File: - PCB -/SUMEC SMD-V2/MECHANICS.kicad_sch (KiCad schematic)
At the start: 9 parts, among them J1 Conn_01x04_Pin, J3 Conn_01x03_Pin, J4 Conn_01x02, SW1 SW_Push

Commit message: cleanup
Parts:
- removed J4: Conn_01x02, Connector_PinHeader_2.54mm:PinHeader_1x02_P2.54mm_Vertical, symbol Connector_Generic:Conn_01x02
- added SW4: SW_DPDT_x2, Connector_PinHeader_2.54mm:PinHeader_1x03_P2.54mm_Vertical, symbol Switch:SW_DPDT_x2
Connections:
- net +8V: now also SW4.2 (B)
- net VBATT: now also SW4.1 (A)
- no-connect marks 0 -> 1
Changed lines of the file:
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@@
     (company "SPŠ NA PROSEKU")
   )
-  (wire (pts (xy 172.72 62.23) (xy 172.72 64.77))
-    (stroke (width 0) (type default))
-  )
+  (no_connect (at 190.5 69.85))
   (wire (pts (xy 173.99 114.3) (xy 182.88 114.3))
     (stroke (width 0) (type default))
   )
-  (wire (pts (xy 172.72 67.31) (xy 175.26 67.31))
+  (wire (pts (xy 187.96 64.77) (xy 185.42 64.77))
     (stroke (width 0) (type default))
   )
@@
     (stroke (width 0) (type default))
   )
+  (wire (pts (xy 173.99 67.31) (xy 175.26 67.31))
+    (stroke (width 0) (type default))
+  )
   (polyline (pts (xy 148.59 44.45) (xy 153.67 44.45))
     (stroke (width 0) (type default))
@@
     (stroke (width 0) (type default))
   )
-  (wire (pts (xy 172.72 64.77) (xy 175.26 64.77))
-    (stroke (width 0) (type default))
-  )
   (wire (pts (xy 173.99 132.08) (xy 185.42 132.08))
     (stroke (width 0) (type default))
@@
   )
   (polyline (pts (xy 64.77 148.59) (xy 143.51 148.59))
+    (stroke (width 0) (type default))
+  )
+  (wire (pts (xy 190.5 69.85) (xy 185.42 69.85))
     (stroke (width 0) (type default))
   )
@@
     (effects (font (size 1.27 1.27) italic) (justify left bottom))
   )
-  (global_label "VBATT" (shape input) (at 172.72 67.31 180) (fields_autoplaced)
-    (effects (font (size 1 1) (color 0 0 0 1)) (justify right))
-    (property "Intersheetrefs" "${INTERSHEET_REFS}" (at 166.1941 67.31 0)
-      (effects (font (size 1.27 1.27)) (justify right) hide)
+  (global_label "VBATT" (shape input) (at 187.96 64.77 0) (fields_autoplaced)
+    (effects (font (size 1 1) (color 0 0 0 1)) (justify left))
+    (property "Intersheetrefs" "${INTERSHEET_REFS}" (at 194.4859 64.77 0)
+      (effects (font (size 1.27 1.27)) (justify left) hide)
     )
   )
@@
     )
   )
-  (symbol (lib_id "power:+8V") (at 172.72 62.23 0) (unit 1)
+  (symbol (lib_id "Switch:SW_DPDT_x2") (at 180.34 67.31 0) (unit 1)
+    (in_bom yes) (on_board yes) (dnp no)
+    (property "Reference" "SW4" (at 180.34 59.69 0)
+      (effects (font (size 1.27 1.27)))
+    )
+    (property "Value" "SW_DPDT_x2" (at 180.34 62.23 0)
+      (effects (font (size 1.27 1.27)))
+    )
+    (property "Footprint" "Connector_PinHeader_2.54mm:PinHeader_1x03_P2.54mm_Vertical" (at 180.34 67.31 0)
+      (effects (font (size 1.27 1.27)) hide)
+    )
+    (property "Datasheet" "~" (at 180.34 67.31 0)
+      (effects (font (size 1.27 1.27)) hide)
+    )
+    (pin "1")
+    (pin "2")
+    (pin "3")
+    (pin "4")
+    (pin "5")
+    (pin "6")
+    (instances
+      (project "sumec"
+        (path "/fc70a1a8-ed7c-4a0f-9b1a-f23293528385/05a35bad-c108-46ad-8f95-76319a60a14f"
+          (reference "SW4") (unit 1)
+        )
+      )
+    )
+  )
+  (symbol (lib_id "power:+8V") (at 173.99 67.31 90) (unit 1)
     (in_bom yes) (on_board yes) (dnp no) (fields_autoplaced)
-    (property "Reference" "#PWR02" (at 172.72 66.04 0)
-      (effects (font (size 1.27 1.27)) hide)
-    )
-    (property "Value" "+8V" (at 172.72 58.42 0)
-      (effects (font (size 1.27 1.27)))
-    )
-    (property "Footprint" "" (at 172.72 62.23 0)
-      (effects (font (size 1.27 1.27)) hide)
-    )
-    (property "Datasheet" "" (at 172.72 62.23 0)
+    (property "Reference" "#PWR02" (at 177.8 67.31 0)
+      (effects (font (size 1.27 1.27)) hide)
+    )
+    (property "Value" "+8V" (at 170.18 67.945 90)
+      (effects (font (size 1.27 1.27)) (justify left))
+    )
+    (property "Footprint" "" (at 173.99 67.31 0)
+      (effects (font (size 1.27 1.27)) hide)
+    )
+    (property "Datasheet" "" (at 173.99 67.31 0)
       (effects (font (size 1.27 1.27)) hide)
     )
@@
         )
       )
-    )
-  )
-  (symbol (lib_id "Connector_Generic:Conn_01x02") (at 180.34 64.77 0) (unit 1)
-    (in_bom yes) (on_board yes) (dnp no) (fields_autoplaced)
-    (property "Reference" "J4" (at 182.88 65.405 0)
-      (effects (font (size 1.27 1.27)) (justify left))
-    )
-    (property "Value" "Conn_01x02" (at 182.88 67.945 0)
-      (effects (font (size 1.27 1.27)) (justify left))
-    )
-    (property "Footprint" "Connector_PinHeader_2.54mm:PinHeader_1x02_P2.54mm_Vertical" (at 180.34 64.77 0)
-      (effects (font (size 1.27 1.27)) hide)
-    )
-    (property "Datasheet" "~" (at 180.34 64.77 0)
-      (effects (font (size 1.27 1.27)) hide)
-    )
-    (pin "1")
-    (pin "2")
-    (instances
-      (project "sumec"
-        (path "/fc70a1a8-ed7c-4a0f-9b1a-f23293528385/05a35bad-c108-46ad-8f95-76319a60a14f"
-          (reference "J4") (unit 1)
-        )
-      )

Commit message: sumec SMD V2 schematic update
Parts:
- removed H? (x4): MountingHole M3, MountingHole:MountingHole_3.2mm_M3_ISO7380_Pad, symbol Mechanical:MountingHole
- removed J3: Conn_01x03_Pin, Connector_PinSocket_2.54mm:PinSocket_1x03_P2.54mm_Vertical, symbol Connector:Conn_01x03_Pin
- added H1, H2, H3, H4: MountingHole_Pad, MountingHole:MountingHole_3.2mm_M3_Pad, symbol Mechanical:MountingHole_Pad
- J1: footprint Connector_PinHeader_2.54mm:PinHeader_1x04_P2.54mm_Vertical -> (none)
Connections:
- net GND: now also H1.1, H2.1, H3.1, H4.1
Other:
- note added: "CONNECTORS"
- note added: "Main switch is at the top of the robot for easy access to the switch."
- note added: "TEST BUTTON"
- note added: "lepsi konektory nez arduino bullshit"
- note added: "vlastni 2,54 footprint a 3D model"
- note removed: "Main switch is connected via two wires for easy access."
- note removed: "PADY a PROKOVY"
- note removed: "Pads for connecting motors and rivets"
- note removed: "TEST TLAČITKO"
- moved on the sheet: J1, J?

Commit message: pcb schematic update
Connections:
- net +8V: no longer names the net of SW4.2 (B)
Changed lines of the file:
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@@
-    )
-  )
-  (symbol (lib_id "power:+8V") (at 173.99 67.31 90) (unit 1)
-    (in_bom yes) (on_board yes) (dnp no) (fields_autoplaced)
-    (property "Reference" "#PWR02" (at 177.8 67.31 0)
-      (effects (font (size 1.27 1.27)) hide)
-    )
-    (property "Value" "+8V" (at 170.18 67.945 90)
-      (effects (font (size 1.27 1.27)) (justify left))
-    )
-    (property "Footprint" "" (at 173.99 67.31 0)
-      (effects (font (size 1.27 1.27)) hide)
-    )
-    (property "Datasheet" "" (at 173.99 67.31 0)
-      (effects (font (size 1.27 1.27)) hide)
-    )
-    (pin "1")
-    (instances
-      (project "sumec"
-        (path "/fc70a1a8-ed7c-4a0f-9b1a-f23293528385/05a35bad-c108-46ad-8f95-76319a60a14f"
-          (reference "#PWR02") (unit 1)
-        )
-      )
     )
   )

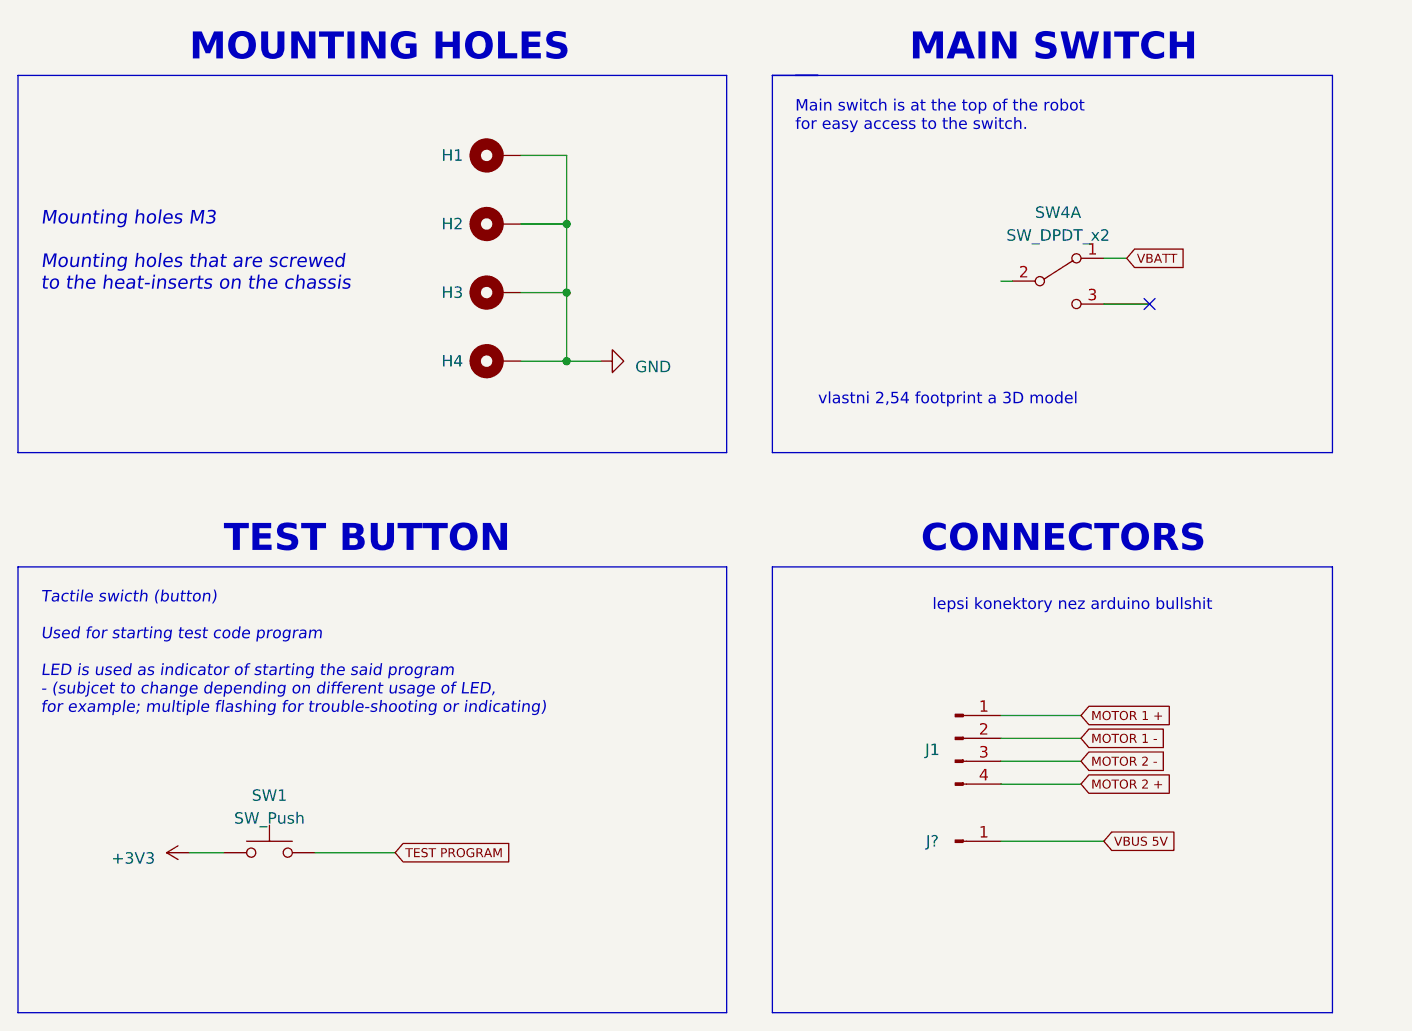
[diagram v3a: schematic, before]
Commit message: SMDV2 - footprints
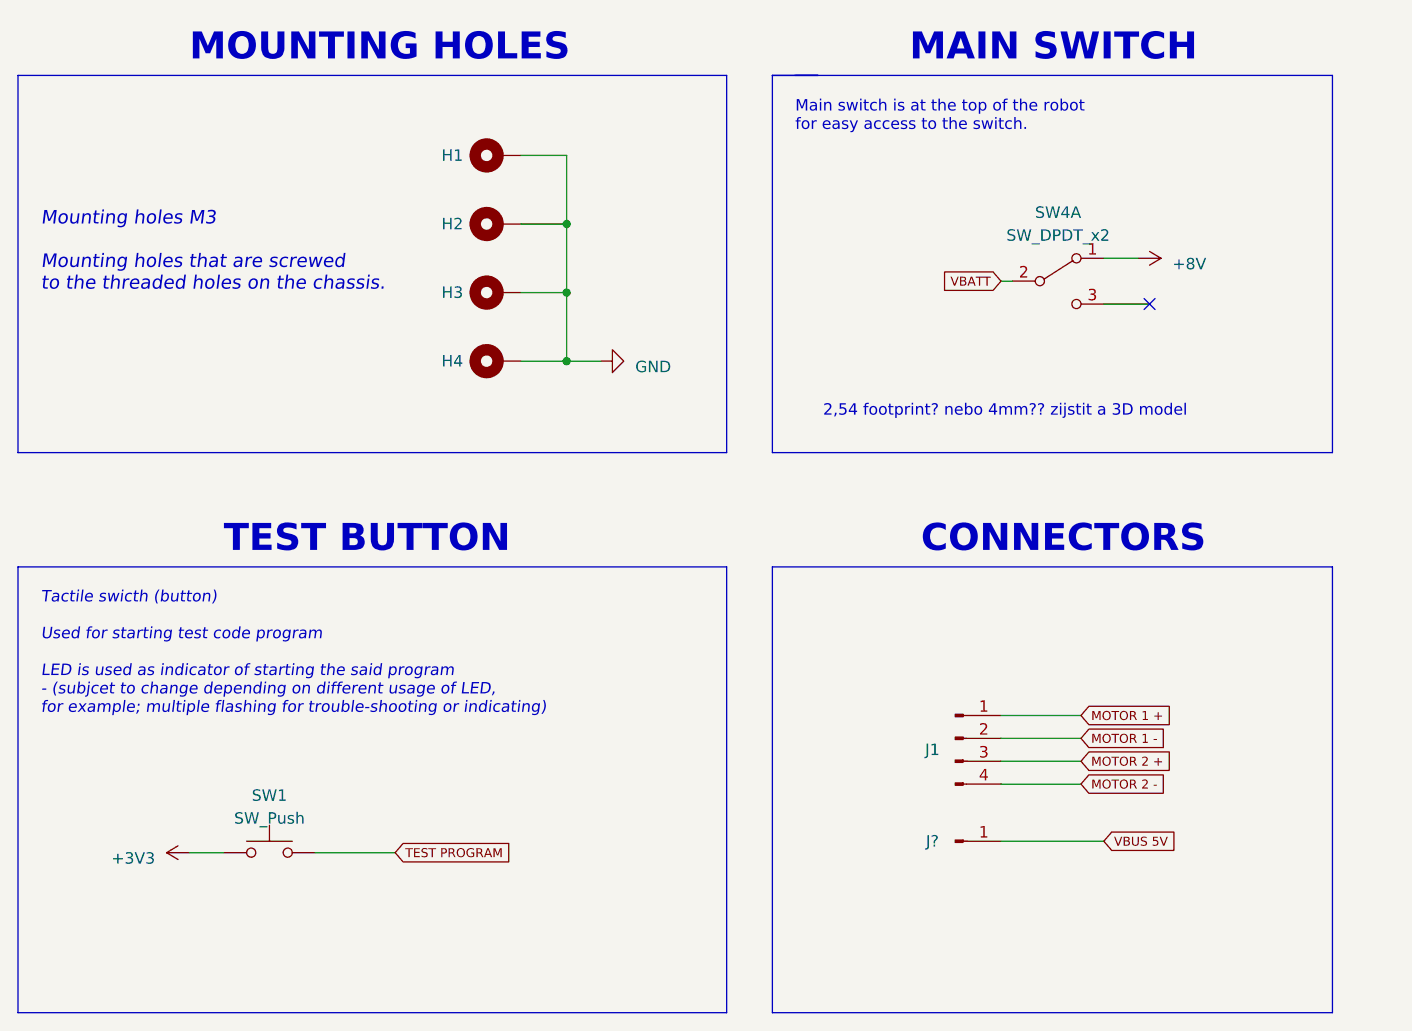
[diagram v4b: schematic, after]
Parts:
- J1: footprint (none) -> Connector_JST:JST_XH_B4B-XH-A_1x04_P2.50mm_Vertical
- SW4: footprint Connector_PinHeader_2.54mm:PinHeader_1x03_P2.54mm_Vertical -> sumec-smdV2_library:Custom_SPDT_Switch
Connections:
- net MOTOR 2 +: now also J1.3 (Pin_3); no longer J1.4 (Pin_4)
- net MOTOR 2 -: now also J1.4 (Pin_4); no longer J1.3 (Pin_3)
- net VBATT: now also SW4.2 (B); no longer SW4.1 (A)
- new net +8V: SW4.1 (A)
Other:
- note added: "2,54 footprint? nebo 4mm?? zijstit a 3D model"
- note added: "Mounting holes M3 Mounting holes that are screwed to the threaded holes on the chassis."
- note removed: "Mounting holes M3 Mounting holes that are screwed to the heat-inserts on the chassis"
- note removed: "lepsi konektory nez arduino bullshit"
- note removed: "vlastni 2,54 footprint a 3D model"
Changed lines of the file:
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@@
     (stroke (width 0) (type default))
   )
-  (wire (pts (xy 187.96 64.77) (xy 185.42 64.77))
+  (wire (pts (xy 189.23 64.77) (xy 185.42 64.77))
     (stroke (width 0) (type default))
   )
@@
   (polyline (pts (xy 64.77 148.59) (xy 64.77 99.06))
     (stroke (width 0) (type default))
-  )
-  (text "lepsi konektory nez arduino bullshit" (at 166.37 104.14 0)
-    (effects (font (size 1.27 1.27) (color 255 0 0 1)) (justify left bottom))
   )
   (text "MOUNTING HOLES" (at 83.82 43.18 0)
     (effects (font (size 3 3) bold (color 0 0 0 1)) (justify left bottom))
   )
-  (text "Mounting holes M3 \n\nMounting holes that are screwed \nto the heat-inserts on the chassis\n"
+  (text "Mounting holes M3 \n\nMounting holes that are screwed \nto the threaded holes on the chassis.\n"
     (at 67.31 68.58 0)
     (effects (font (size 1.5 1.5) italic) (justify left bottom))
@@
     (effects (font (size 1.27 1.27) italic) (justify left bottom))
   )
-  (text "vlastni 2,54 footprint a 3D model" (at 153.67 81.28 0)
+  (text " 2,54 footprint? nebo 4mm?? zijstit a 3D model" (at 153.67 82.55 0)
     (effects (font (size 1.27 1.27) (color 255 0 0 1)) (justify left bottom))
   )
-  (global_label "VBATT" (shape input) (at 187.96 64.77 0) (fields_autoplaced)
-    (effects (font (size 1 1) (color 0 0 0 1)) (justify left))
-    (property "Intersheetrefs" "${INTERSHEET_REFS}" (at 194.4859 64.77 0)
-      (effects (font (size 1.27 1.27)) (justify left) hide)
-    )
-  )
   (global_label "VBUS 5V" (shape input) (at 185.42 129.54 0) (fields_autoplaced)
     (effects (font (size 1 1) (color 0 0 0 1)) (justify left))
@@
     )
   )
+  (global_label "MOTOR 2 -" (shape input) (at 182.88 123.19 0) (fields_autoplaced)
+    (effects (font (size 1 1) (color 0 0 0 1)) (justify left))
+    (property "Intersheetrefs" "${INTERSHEET_REFS}" (at 193.8822 123.19 0)
+      (effects (font (size 1.27 1.27)) (justify left) hide)
+    )
+  )
   (global_label "MOTOR 1 -" (shape input) (at 182.88 118.11 0) (fields_autoplaced)
     (effects (font (size 1 1) (color 0 0 0 1)) (justify left))
@@
     )
   )
-  (global_label "MOTOR 2 -" (shape input) (at 182.88 120.65 0) (fields_autoplaced)
+  (global_label "MOTOR 2 +" (shape input) (at 182.88 120.65 0) (fields_autoplaced)
     (effects (font (size 1 1) (color 0 0 0 1)) (justify left))
     (property "Intersheetrefs" "${INTERSHEET_REFS}" (at 193.8822 120.65 0)
@@
     )
   )
+  (global_label "VBATT" (shape input) (at 173.99 67.31 180) (fields_autoplaced)
+    (effects (font (size 1 1) (color 0 0 0 1)) (justify right))
+    (property "Intersheetrefs" "${INTERSHEET_REFS}" (at 167.4641 67.31 0)
+      (effects (font (size 1.27 1.27)) (justify right) hide)
+    )
+  )
   (global_label "TEST PROGRAM" (shape input) (at 106.68 130.81 0) (fields_autoplaced)
     (effects (font (size 1 1) (color 0 0 0 1)) (justify left))
@@
     (effects (font (size 1 1) (color 0 0 0 1)) (justify left))
     (property "Intersheetrefs" "${INTERSHEET_REFS}" (at 193.8822 115.57 0)
-      (effects (font (size 1.27 1.27)) (justify left) hide)
-    )
-  )
-  (global_label "MOTOR 2 +" (shape input) (at 182.88 123.19 0) (fields_autoplaced)
-    (effects (font (size 1 1) (color 0 0 0 1)) (justify left))
-    (property "Intersheetrefs" "${INTERSHEET_REFS}" (at 193.8822 123.19 0)
       (effects (font (size 1.27 1.27)) (justify left) hide)
     )
@@
       (effects (font (size 1.27 1.27)) hide)
     )
-    (property "Footprint" "" (at 168.91 118.11 0)
+    (property "Footprint" "Connector_JST:JST_XH_B4B-XH-A_1x04_P2.50mm_Vertical" (at 168.91 118.11 0)
       (effects (font (size 1.27 1.27)) hide)
     )
@@
     )
   )
+  (symbol (lib_id "power:+8V") (at 189.23 64.77 270) (unit 1)
+    (in_bom yes) (on_board yes) (dnp no) (fields_autoplaced)
+    (property "Reference" "#PWR048" (at 185.42 64.77 0)
+      (effects (font (size 1.27 1.27)) hide)
+    )
+    (property "Value" "+8V" (at 193.04 65.405 90)
+      (effects (font (size 1.27 1.27)) (justify left))
+    )
+    (property "Footprint" "" (at 189.23 64.77 0)
+      (effects (font (size 1.27 1.27)) hide)
+    )
+    (property "Datasheet" "" (at 189.23 64.77 0)
+      (effects (font (size 1.27 1.27)) hide)
+    )
+    (pin "1")
+    (instances
+      (project "sumec"
+        (path "/fc70a1a8-ed7c-4a0f-9b1a-f23293528385/05a35bad-c108-46ad-8f95-76319a60a14f"
+          (reference "#PWR048") (unit 1)
+        )
+        (path "/fc70a1a8-ed7c-4a0f-9b1a-f23293528385/11aa20d4-c4ff-49be-9179-c2911da50f67"
+          (reference "#PWR047") (unit 1)
+        )
+      )
+    )
+  )
   (symbol (lib_id "power:+3V3") (at 83.82 130.81 90) (unit 1)
     (in_bom yes) (on_board yes) (dnp no) (fields_autoplaced)
@@
       (effects (font (size 1.27 1.27)))
     )
-    (property "Footprint" "Connector_PinHeader_2.54mm:PinHeader_1x03_P2.54mm_Vertical" (at 180.34 67.31 0)
-      (effects (font (size 1.27 1.27)) hide)
-    )
+    (property "Footprint" "sumec-smdV2_library:Custom_SPDT_Switch" (at 180.34 67.31 0)
+      (effects (font (size 1.27 1.27)) hide)
+    )
